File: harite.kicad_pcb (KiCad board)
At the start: 0 parts

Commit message: Layout switches
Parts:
- added D1: D, footprints:D_SOD123, F.Cu at (97.5, 59.2)
- added D10: D, footprints:D_SOD123, F.Cu at (106.1, 77.5)
- added D11: D, footprints:D_SOD123, F.Cu at (106.1, 81.1)
- added D12: D, footprints:D_SOD123, F.Cu at (106.1, 84.7)
- added D13: D, footprints:D_SOD123, F.Cu at (106.1, 88.3)
- added D14: D, footprints:D_SOD123, F.Cu at (106.1, 91.9)
- added D15: D, footprints:D_SOD123, F.Cu at (106.1, 95.5)
- added D16: D, footprints:D_SOD123, F.Cu at (106.1, 99.1)
- added D17: D, footprints:D_SOD123, F.Cu at (113.3, 73.9)
- added D18: D, footprints:D_SOD123, F.Cu at (113.3, 77.5)
- added D19: D, footprints:D_SOD123, F.Cu at (113.3, 81.1)
- added D2: D, footprints:D_SOD123, F.Cu at (102.5, 59.2)
- added D20: D, footprints:D_SOD123, F.Cu at (113.3, 84.7)
- added D21: D, footprints:D_SOD123, F.Cu at (113.3, 88.3)
- added D22: D, footprints:D_SOD123, F.Cu at (113.3, 91.9)
- added D23: D, footprints:D_SOD123, F.Cu at (113.3, 95.5)
- added D24: D, footprints:D_SOD123, F.Cu at (113.3, 99.1)
- added D25: D, footprints:D_SOD123, F.Cu at (120.5, 73.9)
- added D3: D, footprints:D_SOD123, F.Cu at (107.5, 59.2)
- added D4: D, footprints:D_SOD123, F.Cu at (112.0, 59.2)
- added D5: D, footprints:D_SOD123, F.Cu at (98.9, 88.3)
- added D6: D, footprints:D_SOD123, F.Cu at (98.9, 91.9)
- added D7: D, footprints:D_SOD123, F.Cu at (98.9, 95.5)
- added D8: D, footprints:D_SOD123, F.Cu at (98.9, 99.1)
- added D9: D, footprints:D_SOD123, F.Cu at (106.1, 73.9)
- added S1: SKRHADE010, footprints:SKRHADE010, F.Cu at (118.7, 43.8)
- added S2: SKRHADE010, footprints:SKRHADE010, F.Cu at (158.8, 31.2)
- added S3: SKRHADE010, footprints:SKRHADE010, F.Cu at (140.3, 36.4)
- added S4: SKRHADE010, footprints:SKRHADE010, F.Cu at (177.1, 38.5)
- added S5: SKRHADE010, footprints:SKRHADE010, F.Cu at (196.0, 85.8)
- added U1: rp2040-zero, footprints:rp2040-zero-tht, F.Cu at (242.4, 45.1)
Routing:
- net Net-(D1-A): track 0.00 -> 23.0 mm
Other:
- board outline added: 12 x 21 mm
- copper layers 0 -> 2

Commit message: pcb
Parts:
- moved D16 100.2 mm to (176.2, 27.5), turned to -90 degrees
- moved D24 92.3 mm to (205.5, 94.8), turned to 90 degrees
- moved D21 82.0 mm to (194.2, 74.8), turned to -90 degrees
- moved D25 81.6 mm to (199.2, 95.2), turned to 90 degrees
- moved D19 80.3 mm to (186.5, 48.1), turned to 90 degrees
- moved D22 77.8 mm to (189.2, 74.8), turned to -90 degrees
- moved D8 77.1 mm to (127.5, 27.5), turned to -90 degrees
- moved D14 76.9 mm to (165.2, 42.7), turned to 90 degrees
- moved D20 76.8 mm to (180.8, 47.9), turned to 90 degrees
- moved D15 76.5 mm to (161.2, 42.5), turned to 90 degrees
- moved D13 75.6 mm to (145.5, 23.7), turned to -90 degrees
- moved D7 75.5 mm to (131.8, 27.5), turned to -90 degrees
- moved D17 74.8 mm to (172.2, 27.8), turned to -90 degrees
- moved D12 74.8 mm to (149.5, 23.8), turned to -90 degrees
- moved D11 74.5 mm to (153.8, 23.8), turned to -90 degrees
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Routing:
- net Net-(D1-A): track 23.0 -> 0.00 mm
- net Net-(D7-A): track 0.00 -> 0.91 mm
- net Net-(D12-A): track 0.00 -> 0.67 mm

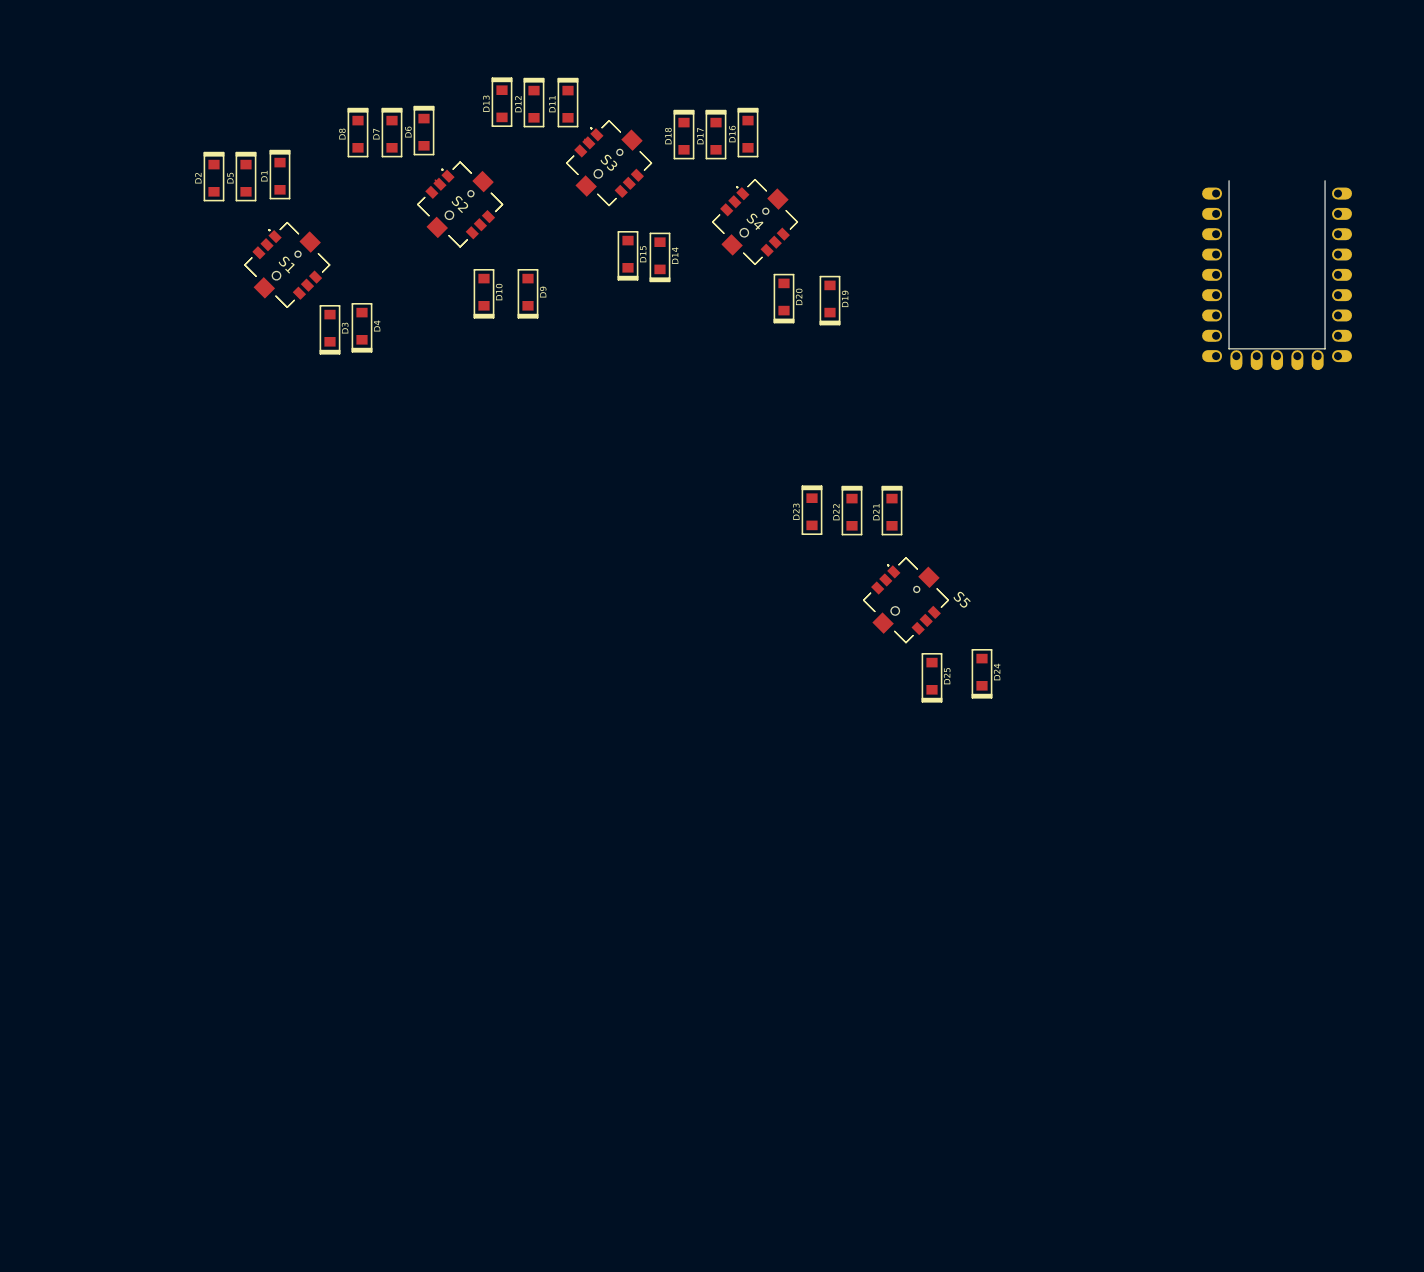
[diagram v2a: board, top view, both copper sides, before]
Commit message: Add scottokeebs
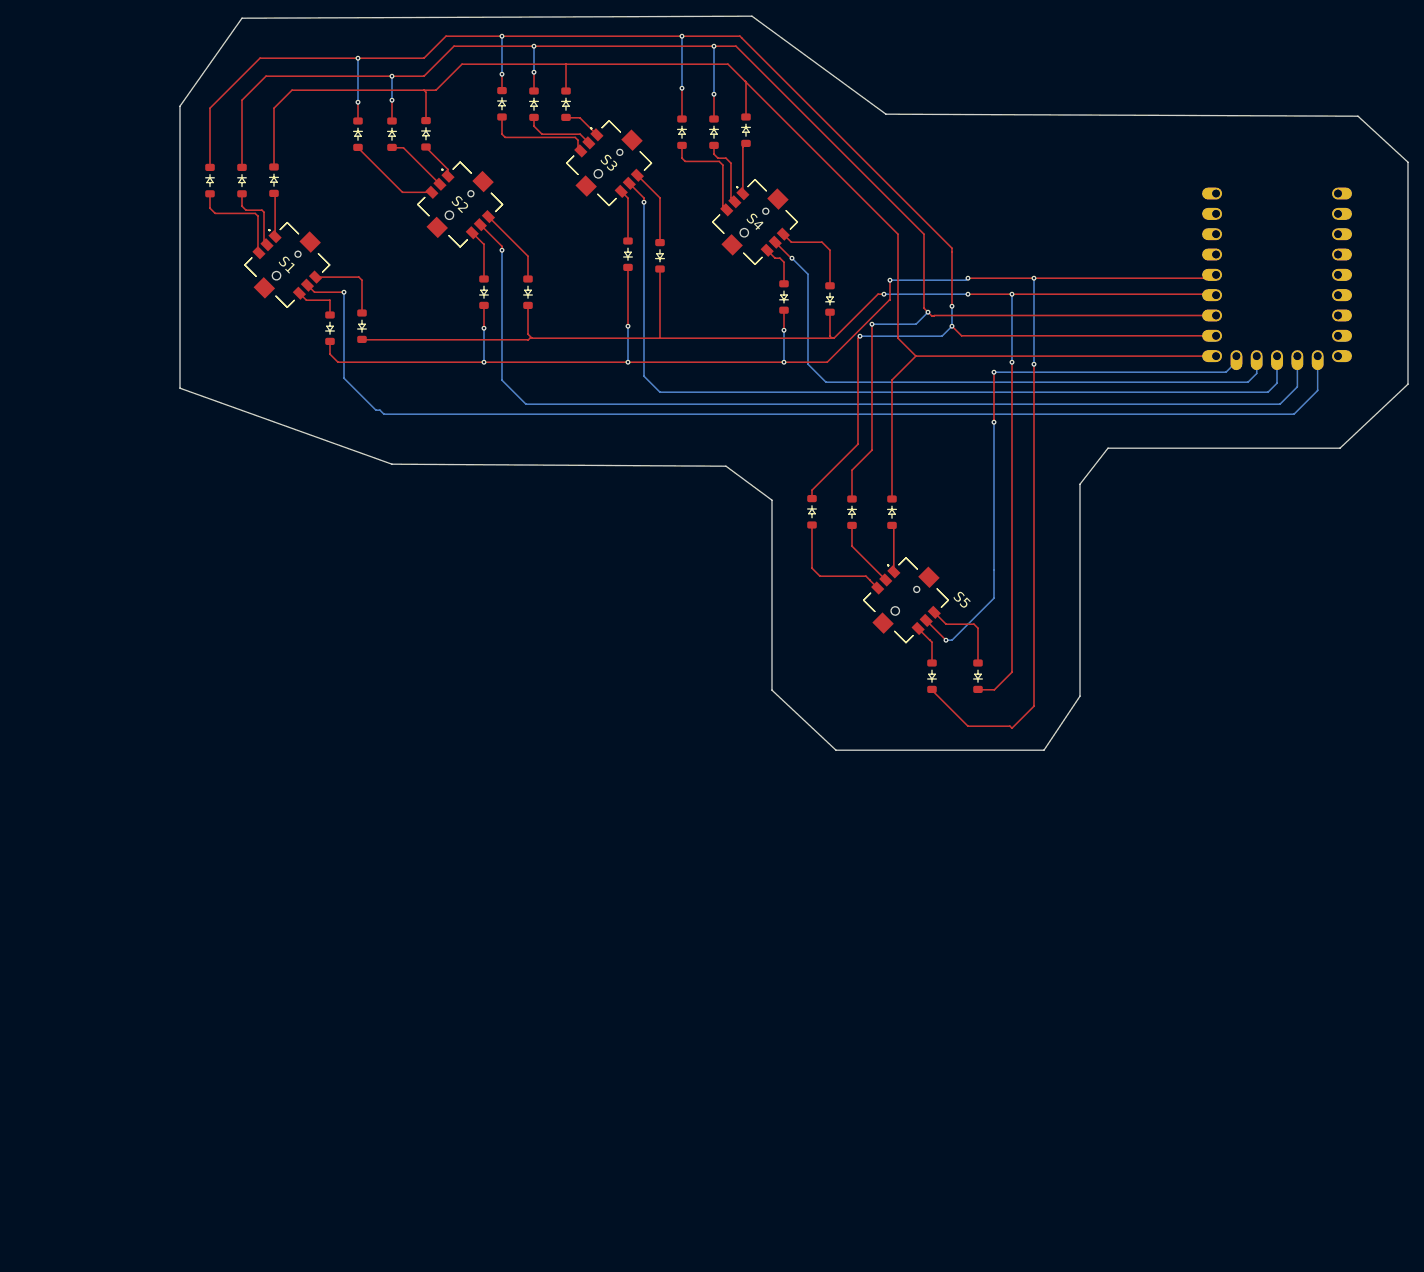
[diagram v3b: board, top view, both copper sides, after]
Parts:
- D1, D10, D11, D12, D13, D14, D15, D16, D17, D18, D19, D2, D20, D21, D22, D23, D24, D25, D3, D4, D5, D6, D7, D8, D9: footprint footprints:D_SOD123 -> ScottoKeebs_Components:Diode_SOD-123
- U1: value rp2040-zero -> RP2040_Zero; footprint footprints:rp2040-zero-tht -> ScottoKeebs_MCU:RP2040_Zero
- moved D1 0.90 mm to (117.0, 33.2)
- moved D24 0.71 mm to (205.0, 95.2)
- moved D2 0.58 mm to (109.0, 33.3)
- moved D5 0.58 mm to (113.0, 33.3)
- moved D16 0.56 mm to (176.0, 27.0)
- moved D17 0.56 mm to (172.0, 27.2)
- moved D18 0.56 mm to (168.0, 27.2)
- moved D6 0.32 mm to (136.0, 27.4)
- moved D11 0.25 mm to (153.5, 23.8)
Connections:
- D2 pad 1: Row 2 -> Row 3
- D3 pad 1: Row 5 -> Row 2
- D5 pad 1: Row 3 -> Row 5
- S1 pad 2: Net-(D5-A) -> Net-(D2-A)
- S1 pad 3: Net-(D2-A) -> Net-(D3-A)
- S1 pad 6: Net-(D3-A) -> Net-(D5-A)
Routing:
- net Row 2: track 0.00 -> 217.7 mm, vias 0 -> 9
- net Row 5: track 0.00 -> 213.4 mm, vias 0 -> 10
- net Row 3: track 0.00 -> 202.9 mm, vias 0 -> 8
- net Row 1: track 0.00 -> 180.7 mm
- net Row 4: track 0.00 -> 177.8 mm, vias 0 -> 4
- net Col 1: track 0.00 -> 144.8 mm, vias 0 -> 1
- net Col 2: track 0.00 -> 126.0 mm, vias 0 -> 1
- net Col 3: track 0.00 -> 108.7 mm, vias 0 -> 1
- net Col 4: track 0.00 -> 76.6 mm, vias 0 -> 1
- net Col 5: track 0.00 -> 71.5 mm, vias 0 -> 3
- net Net-(D23-A): track 0.00 -> 14.6 mm
- net Net-(D13-A): track 0.00 -> 13.4 mm
- net Net-(D18-A): track 0.00 -> 12.8 mm
- net Net-(D2-A): track 0.00 -> 12.8 mm
- net Net-(D8-A): track 0.00 -> 11.5 mm
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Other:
- board size 12 x 21 mm -> 153.5 x 91.8 mm

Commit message: Add trrs
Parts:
- added U2: TRRS, ScottoKeebs_Components:TRRS_PJ-320A, F.Cu at (252.1, 69.8)
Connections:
- D12 pad 1: Row 3 -> Row 2
- D13 pad 1: Row 2 -> Row 3
- D17 pad 1: Row 3 -> Row 2
- D18 pad 1: Row 2 -> Row 3
- D2 pad 1: Row 3 -> Row 2
- D22 pad 1: Row 3 -> Row 2
- D23 pad 1: Row 2 -> Row 3
- D3 pad 1: Row 2 -> Row 3
- D7 pad 1: Row 3 -> Row 2
- D8 pad 1: Row 2 -> Row 3
- U1 pad 1: unconnected-(U1-0-Pad1) -> GP0
- U1 pad 2: unconnected-(U1-1-Pad2) -> GP1
- U1 pad 21: unconnected-(U1-3V3-Pad21) -> 3V3
- U1 pad 22: unconnected-(U1-GND-Pad22) -> GND
- U1 pad 23: unconnected-(U1-5V-Pad23) -> 5V
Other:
- outline, holes or cut-outs redrawn

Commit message: update usbc
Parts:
- removed U2: TRRS, ScottoKeebs_Components:TRRS_PJ-320A
- added Cirque1: Cirque, footprints:CIRQUE-TM040040, F.Cu at (149.7, 80.2)
- added D26: D, ScottoKeebs_Components:Diode_SOD-123, F.Cu at (187.5, 107.1)
- added D27: D, ScottoKeebs_Components:Diode_SOD-123, F.Cu at (187.5, 110.4)
- added D28: D, ScottoKeebs_Components:Diode_SOD-123, F.Cu at (187.5, 113.8)
- added D29: D, ScottoKeebs_Components:Diode_SOD-123, F.Cu at (187.5, 117.1)
- added D30: D, ScottoKeebs_Components:Diode_SOD-123, F.Cu at (187.5, 120.5)
- added S6: SKRHADE010, footprints:SKRHADE010, F.Cu at (196.1, 111.9)
- added USB1: HRO-TYPE-C-31-M-12, footprints:HRO-TYPE-C-31-M-12, F.Cu at (252.3, 75.3)
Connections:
- U1 pad 10: Col 1 -> Col 2
- U1 pad 11: Col 2 -> Col 3
- U1 pad 12: Col 3 -> Col 4
- U1 pad 13: Col 4 -> Col 5
- U1 pad 14: Col 5 -> Col 6
- U1 pad 3: unconnected-(U1-2-Pad3) -> SCK
- U1 pad 4: unconnected-(U1-3-Pad4) -> SI
- U1 pad 5: unconnected-(U1-4-Pad5) -> SO
- U1 pad 6: unconnected-(U1-5-Pad6) -> SS
- U1 pad 9: unconnected-(U1-8-Pad9) -> Col 1
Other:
- board size 153.5 x 91.8 mm -> 153.5 x 121.8 mm

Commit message: Fix usb
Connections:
- USB1 pad 11: unconnected-(USB1-VBUS-Pad11) -> 5V
- USB1 pad 6: GP0 -> GP1
- USB1 pad 7: GP1 -> GP0
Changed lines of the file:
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@@
 	(net 67 "SO")
 	(net 68 "unconnected-(USB1-CC1-Pad4)")
-	(net 69 "unconnected-(USB1-VBUS-Pad11)")
-	(net 70 "unconnected-(USB1-CC2-Pad10)")
-	(net 71 "unconnected-(USB1-SBU1-Pad9)")
-	(net 72 "unconnected-(USB1-SBU2-Pad3)")
+	(net 69 "unconnected-(USB1-CC2-Pad10)")
+	(net 70 "unconnected-(USB1-SBU1-Pad9)")
+	(net 71 "unconnected-(USB1-SBU2-Pad3)")
 	(footprint "ScottoKeebs_Components:Diode_SOD-123"
 		(layer "F.Cu")
@@
 			(size 0.3 1.45)
 			(layers "F.Cu" "F.Paste" "F.Mask")
-			(net 72 "unconnected-(USB1-SBU2-Pad3)")
+			(net 71 "unconnected-(USB1-SBU2-Pad3)")
 			(pinfunction "SBU2")
 			(pintype "input")
@@
 			(size 0.3 1.45)
 			(layers "F.Cu" "F.Paste" "F.Mask")
-			(net 48 "GP0")
+			(net 50 "GP1")
 			(pinfunction "DP1")
 			(pintype "input")
@@
 			(size 0.3 1.45)
 			(layers "F.Cu" "F.Paste" "F.Mask")
-			(net 50 "GP1")
+			(net 48 "GP0")
 			(pinfunction "DN1")
 			(pintype "input")
@@
 			(size 0.3 1.45)
 			(layers "F.Cu" "F.Paste" "F.Mask")
-			(net 71 "unconnected-(USB1-SBU1-Pad9)")
+			(net 70 "unconnected-(USB1-SBU1-Pad9)")
 			(pinfunction "SBU1")
 			(pintype "input")
@@
 			(size 0.3 1.45)
 			(layers "F.Cu" "F.Paste" "F.Mask")
-			(net 70 "unconnected-(USB1-CC2-Pad10)")
+			(net 69 "unconnected-(USB1-CC2-Pad10)")
 			(pinfunction "CC2")
 			(pintype "input")
@@
 			(size 0.6 1.45)
 			(layers "F.Cu" "F.Paste" "F.Mask")
-			(net 69 "unconnected-(USB1-VBUS-Pad11)")
+			(net 52 "5V")
 			(pinfunction "VBUS")
 			(pintype "input")

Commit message: Shaping
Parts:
- removed D26, D27, D28, D29, D30: D, ScottoKeebs_Components:Diode_SOD-123
- removed S6: SKRHADE010, footprints:SKRHADE010
- moved D5 75.4 mm to (104.8, 108.2), turned to 135 degrees
- moved D23 68.0 mm to (187.3, 142.6), turned to -45 degrees
- moved D22 65.8 mm to (189.5, 140.5), turned to -45 degrees
- moved U1 64.7 mm to (201.2, 95.0)
- moved D21 63.8 mm to (191.2, 138.5), turned to -45 degrees
- moved D2 63.2 mm to (93.2, 94.5), turned to -45 degrees
- moved D1 63.1 mm to (95.2, 92.5), turned to -45 degrees
- moved S5 61.3 mm to (195.0, 147.0)
- moved D18 60.8 mm to (166.8, 88.1), turned to -45 degrees
- moved S1 59.2 mm to (100.0, 100.0)
- moved D17 58.9 mm to (168.6, 86.1), turned to -45 degrees
- moved D25 58.8 mm to (199.5, 154.0), turned to 135 degrees
- moved D16 57.5 mm to (170.5, 84.2), turned to -45 degrees
- moved D4 57.3 mm to (108.2, 105.2), turned to 135 degrees
- moved USB1 56.9 mm to (213.8, 117.2)
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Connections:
- U1 pad 10: Col 2 -> Col 1
- U1 pad 11: Col 3 -> Col 2
- U1 pad 12: Col 4 -> Col 3
- U1 pad 13: Col 5 -> Col 4
- U1 pad 14: Col 6 -> Col 5
- U1 pad 9: Col 1 -> unconnected-(U1-8-Pad9)
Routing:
- net Row 2: track 217.7 -> 0.00 mm, vias 9 -> 0
- net Row 5: track 213.4 -> 0.00 mm, vias 10 -> 0
- net Row 3: track 202.9 -> 0.00 mm, vias 8 -> 0
- net Row 1: track 180.7 -> 0.00 mm
- net Row 4: track 177.8 -> 0.00 mm, vias 4 -> 0
- net Col 1: track 144.8 -> 0.00 mm, vias 1 -> 0
- net Col 2: track 126.0 -> 0.00 mm, vias 1 -> 0
- net Col 3: track 108.7 -> 0.00 mm, vias 1 -> 0
- net Col 4: track 76.6 -> 0.00 mm, vias 1 -> 0
- net Col 5: track 71.5 -> 0.00 mm, vias 3 -> 0
- net Net-(D23-A): track 14.6 -> 0.00 mm
- net Net-(D13-A): track 13.4 -> 0.00 mm
- net Net-(D18-A): track 12.8 -> 0.00 mm
- net Net-(D2-A): track 12.8 -> 0.00 mm
- net Net-(D8-A): track 11.5 -> 0.00 mm
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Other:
- board size 153.5 x 121.8 mm -> 125 x 91.8 mm

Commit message: Tracks
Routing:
- net Row 3: track 0.00 -> 187.7 mm, vias 0 -> 8
- net Row 5: track 0.00 -> 181.6 mm, vias 0 -> 8
- net Row 2: track 0.00 -> 174.1 mm, vias 0 -> 6
- net Row 1: track 0.00 -> 167.2 mm
- net Row 4: track 0.00 -> 167.1 mm, vias 0 -> 4
- net Col 1: track 0.00 -> 120.7 mm, vias 0 -> 1
- net Col 2: track 0.00 -> 87.7 mm, vias 0 -> 1
- net Col 5: track 0.00 -> 64.5 mm
- net Col 3: track 0.00 -> 60.8 mm, vias 0 -> 1
- net 5V: track 0.00 -> 54.3 mm
- net GP0: track 0.00 -> 41.3 mm
- net GP1: track 0.00 -> 38.2 mm
- net Col 4: track 0.00 -> 30.0 mm, vias 0 -> 1
- net Net-(D4-A): track 0.00 -> 4.61 mm
- net Net-(D5-A): track 0.00 -> 4.40 mm
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- added copper zone on B.Cu, net GND
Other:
- board size 125 x 91.8 mm -> 126.5 x 92.8 mm
